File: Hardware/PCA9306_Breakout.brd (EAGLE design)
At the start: 17.8 x 10.2 mm, 15 parts

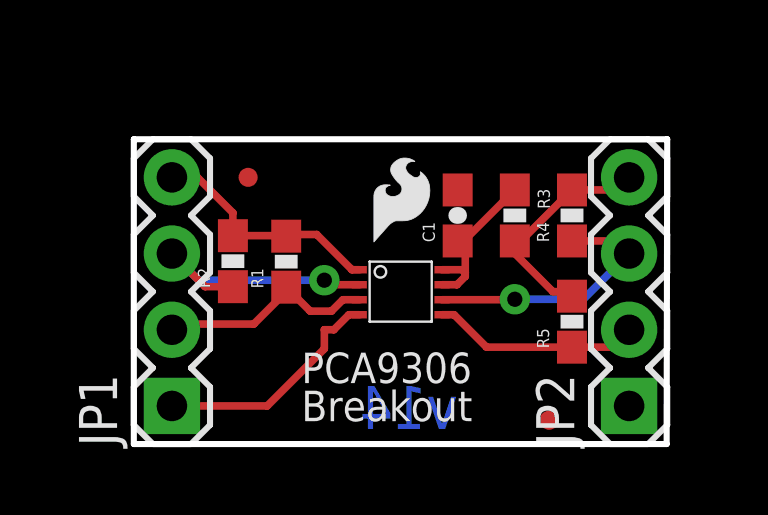
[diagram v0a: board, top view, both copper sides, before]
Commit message: Adds slik lables, adds jumper for enable pin, increases size by 10 mils in both x and y direction, updates PCA9306 to new package
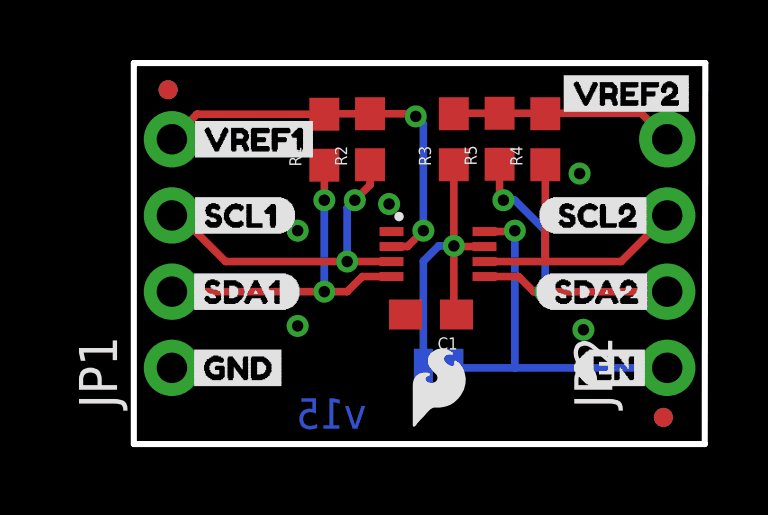
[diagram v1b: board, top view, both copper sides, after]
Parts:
- removed JP4: LOGO-SFESK, SparkFun:SFE-LOGO-FLAME
- removed JP7, JP8: FIDUCIAL1X2.5, abes:FIDUCIAL-1X2.5
- added FD1, FD2, FD3, FD4: FIDUCIALUFIDUCIAL, SparkFun-Aesthetics:FIDUCIAL-MICRO
- added LOGO2: SFE_LOGO_FLAME.1_INCH, SparkFun-Aesthetics:SFE_LOGO_FLAME_.1
- added LOGO3: SFE_LOGO_NAME.1_INCH, SparkFun-Aesthetics:SFE_LOGO_NAME_.1
- added U$10: (no value), EN:EN1
- added U$12: (no value), Product Name:LOGIC_LEVEL0
- added U$13: (no value), Product Name:TRANSLATOR1
- added U$14: (no value), Product Name:PCA93062
- added U$2: (no value), VREF1:VREF13
- added U$3: (no value), VREF1:SCL11
- added U$4: (no value), VREF1:SDA10
- added U$5: (no value), VREF1:GND2
- added U$6: (no value), VREF2:VREF20
- added U$7: (no value), VREF2:SCL22
- added U$8: (no value), VREF2:SDA21
- added U$9: (no value), EN:EN0
- C1: device SparkFun:0603-CAP -> SparkFun-Capacitors:0603
- JP1, JP2: device SparkFun:1X04 -> SparkFun-Connectors:1X04_NO_SILK
- JP3: value LOGO-SFESK -> EN; device SparkFun:SFE-LOGO-FLAME -> SparkFun-Jumpers:SMT-JUMPER_2_NC_TRACE_SILK
- R1, R2, R3, R4, R5: device SparkFun:0603-RES -> SparkFun-Resistors:0603
- U$1: value (none) -> PCA9306; device SparkFun-DigitalIC:PSOP-8 -> SparkFun-IC-Comms:VSSOP_8PIN
- moved LOGO1 6.75 mm to (15.2, 1.52)
- moved R5 6.56 mm to (12.2, 10.2)
- moved R2 6.12 mm to (7.87, 10.2)
- moved JP3 4.71 mm to (10.2, 2.54), flipped to the bottom
- moved R1 4.26 mm to (6.35, 10.1)
- moved C1 3.42 mm to (9.91, 4.32), turned to 180 degrees
- moved R3 3.25 mm to (10.7, 10.2), turned to 90 degrees
- moved R4 2.69 mm to (13.7, 10.2)
- moved JP2 1.80 mm to (17.8, 2.54)
- moved U$1 1.80 mm to (10.2, 6.35), turned to 0 degrees
- moved JP1 1.27 mm to (1.27, 2.54)
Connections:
- removed net NC: JP2.1
- removed net VREF_2: JP2.4, R3.2, R4.2, R5.2
- new net EN: JP2.1, JP3.1, U$1.P8
- new net VREF2_IN: C1.1, JP3.2, R3.1, U$1.P7
- net GND: now also U$1.P1; no longer U$1.4
- net SCL1: now also U$1.P3; no longer U$1.2
- net SCL2: now also U$1.P6; no longer U$1.6
- net SDA1: now also U$1.P4; no longer U$1.3
- net SDA2: now also U$1.P5; no longer U$1.5
- net VREF1: now also U$1.P2; no longer U$1.1
- net VREF2: now also JP2.4, R3.2, R4.2, R5.2; no longer C1.1, R3.1, U$1.7, U$1.8
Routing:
- net EN: track 0.00 -> 12.7 mm, vias 0 -> 1
- net VREF2_IN: track 0.00 -> 10.8 mm, vias 0 -> 1
- net GND: track 7.88 -> 0.00 mm, vias 0 -> 5
- net VREF_2: track 7.60 -> 0.00 mm
- net VREF1: track 8.02 -> 13.7 mm, vias 0 -> 2
- net SDA2: track 6.93 -> 11.4 mm, vias 0 -> 2
- net SDA1: track 7.41 -> 11.7 mm, vias 0 -> 2
- net SCL1: track 9.17 -> 11.5 mm, vias 1 -> 2
- net VREF2: track 5.61 -> 7.50 mm
- net SCL2: track 8.96 -> 9.95 mm, vias 1 -> 0
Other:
- board size 17.8 x 10.2 mm -> 19.1 x 12.7 mm
- board text added: "Revised by: Elias Santistevan"
- board text added: "Toni Klopfenstein"
- board text added: "Units in Inches"
- board text added: "v15"
- board text removed: "Breakout"
- board text removed: "GND"
- board text removed: "NC"
- board text removed: "PCA9306"
- board text removed: "SCL1"
- board text removed: "SCL2"
- board text removed: "SDA1"
- board text removed: "SDA2"
- board text removed: "VREF1"
- board text removed: "VREF2"
- board text removed: "v14"

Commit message: Adds an additional PTH header for GND on VREF2 side
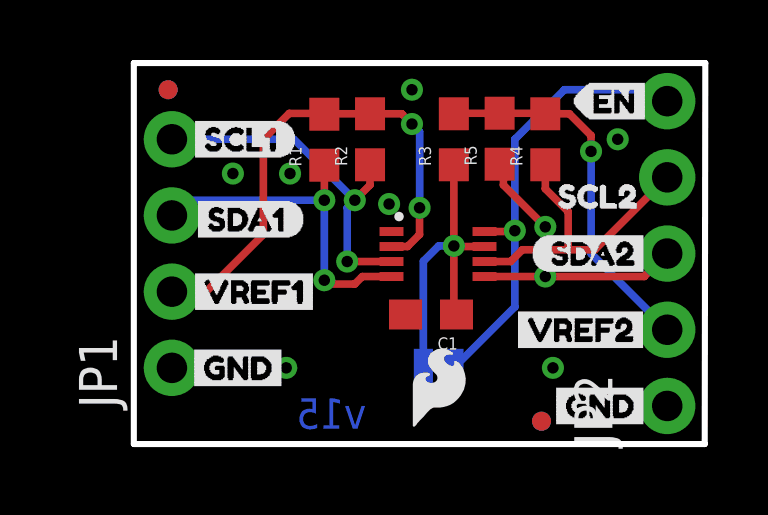
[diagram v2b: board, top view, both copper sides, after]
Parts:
- removed U$7: (no value), VREF2:SCL22
- added U$11: (no value), VREF1:GND2
- added U$15: (no value), SCL2:SCL20
- JP2: device SparkFun-Connectors:1X04_NO_SILK -> SparkFun-Connectors:1X05_NO_SILK
- moved U$9 8.89 mm to (14.6, 11.4)
- moved U$6 8.02 mm to (12.4, 3.81)
- moved U$2 5.08 mm to (1.65, 5.08)
- moved FD3 4.07 mm to (13.6, 0.76)
- moved FD4 4.07 mm to (13.6, 0.76)
- moved U$3 2.54 mm to (1.65, 10.2)
- moved U$4 2.42 mm to (1.78, 7.49)
- moved U$8 1.28 mm to (13.2, 6.35)
- moved JP2 1.27 mm to (17.8, 1.27)
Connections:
- net EN: now also JP2.5; no longer JP2.1
- net GND: now also JP2.1
- net SCL1: now also JP1.4; no longer JP1.3
- net SCL2: now also JP2.4; no longer JP2.3
- net SDA1: now also JP1.3; no longer JP1.2
- net SDA2: now also JP2.3; no longer JP2.2
- net VREF1: now also JP1.2; no longer JP1.4
- net VREF2: now also JP2.2; no longer JP2.4
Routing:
- net VREF2: track 7.50 -> 12.4 mm, vias 0 -> 1
- net VREF1: track 13.7 -> 17.4 mm
- net EN: track 12.7 -> 15.4 mm
- net SDA2: track 11.4 -> 10.8 mm

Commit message: Moves Open Hardware symbol
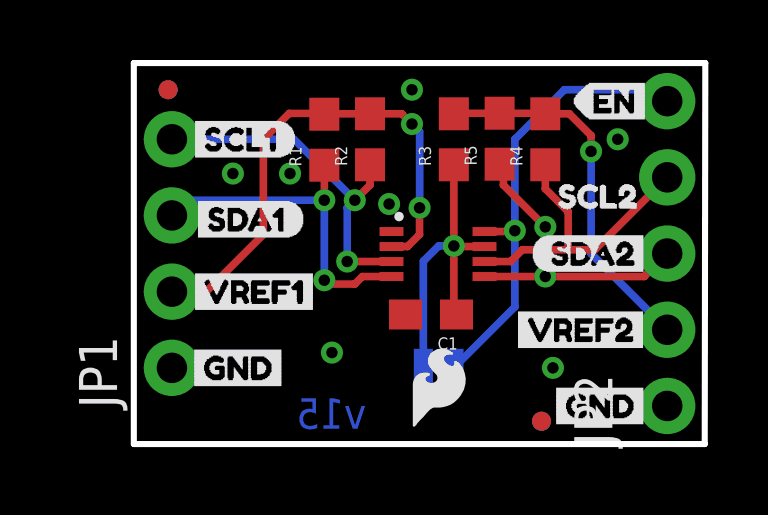
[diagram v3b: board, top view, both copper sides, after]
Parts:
- moved LOGO1 10.4 mm to (4.83, 1.52)
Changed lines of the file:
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@@
 <?xml version="1.0" encoding="utf-8"?>
 <!DOCTYPE eagle SYSTEM "eagle.dtd">
-<eagle version="9.4.2">
+<eagle version="9.4.0">
 <drawing>
 <settings>
@@
 <setting verticaltext="up"/>
 </settings>
-<grid distance="0.05" unitdist="inch" unit="inch" style="lines" multiple="1" display="yes" altdistance="0.005" altunitdist="inch" altunit="inch"/>
+<grid distance="0.01" unitdist="inch" unit="inch" style="lines" multiple="1" display="yes" altdistance="0.001" altunitdist="inch" altunit="inch"/>
 <layers>
 <layer number="1" name="Top" color="4" fill="1" visible="yes" active="yes"/>
@@
 <layer number="14" name="Route14" color="1" fill="6" visible="no" active="no"/>
 <layer number="15" name="Route15" color="4" fill="6" visible="no" active="no"/>
-<layer number="16" name="Bottom" color="1" fill="1" visible="yes" active="yes"/>
-<layer number="17" name="Pads" color="2" fill="1" visible="yes" active="yes"/>
+<layer number="16" name="Bottom" color="31" fill="1" visible="yes" active="yes"/>
+<layer number="17" name="Pads" color="30" fill="1" visible="yes" active="yes"/>
 <layer number="18" name="Vias" color="2" fill="1" visible="yes" active="yes"/>
 <layer number="19" name="Unrouted" color="6" fill="1" visible="yes" active="yes"/>
@@
 <attribute name="VALUE" x="20.955" y="0" size="1.27" layer="27" rot="R90"/>
 </element>
-<element name="LOGO1" library="SparkFun-Aesthetics" package="OSHW-LOGO-S" value="OSHW-LOGOS" x="15.24" y="1.524" smashed="yes" rot="MR0"/>
+<element name="LOGO1" library="SparkFun-Aesthetics" package="OSHW-LOGO-S" value="OSHW-LOGOS" x="4.826" y="1.524" smashed="yes" rot="MR0"/>
 <element name="FRAME1" library="SparkFun-Aesthetics" package="CREATIVE_COMMONS" value="FRAME-LETTER" x="-4.9415875" y="-10.16" smashed="yes">
 <attribute name="DESIGNER" value="" x="-4.9415875" y="-10.16" size="1.778" layer="27" display="off"/>
@@
 <contactref element="JP1" pad="1"/>
 <via x="8.509" y="8.001" extent="1-16" drill="0.381"/>
-<via x="5.08" y="2.54" extent="1-16" drill="0.381"/>
+<via x="6.604" y="3.048" extent="1-16" drill="0.381"/>
 <contactref element="JP2" pad="1"/>
 <via x="9.271" y="11.811" extent="1-16" drill="0.381"/>

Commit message: Moves passives to lower half of board, resulting in full retrace of board....
*Adds HIGH/LOW silk to board
*Adds triple jumper to correctly add enable feature
*Changes 0.1uF capacitor to 100pF capacitor
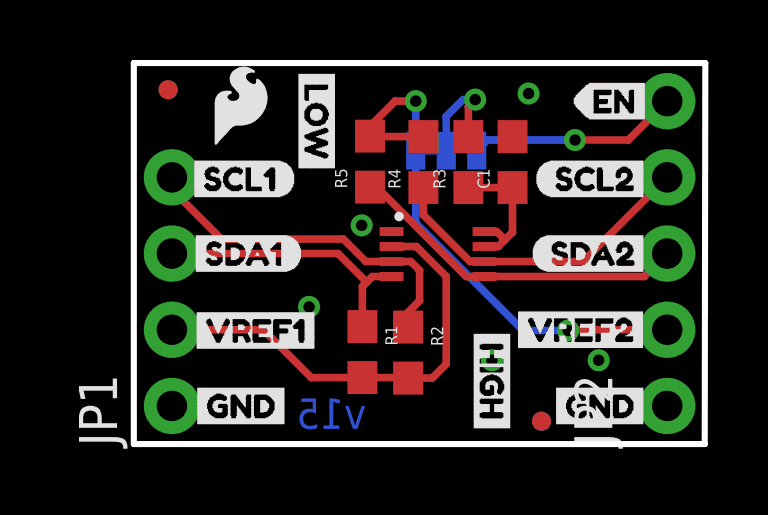
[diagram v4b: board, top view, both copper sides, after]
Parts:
- removed JP3: EN, SparkFun-Jumpers:SMT-JUMPER_2_NC_TRACE_SILK
- added JP4: EN, SparkFun-Jumpers:SMT-JUMPER_3_1-NC_TRACE_SILK
- added U$16: (no value), Jumper_Instru:CLOSE1
- added U$17, U$19: (no value), SIDE:HIGH0
- added U$18, U$20: (no value), SIDE:LOW1
- added U$7: (no value), SCL2:SCL20
- C1: value 0.1uF -> 100pF
- LOGO1: value OSHW-LOGOS -> OSHW-LOGOMINI; device SparkFun-Aesthetics:OSHW-LOGO-S -> SparkFun-Aesthetics:OSHW-LOGO-MINI
- U$15: device SCL2:SCL20 -> Jumper_Instru:CUT0
- moved LOGO2 11.5 mm to (3.56, 11.3)
- moved U$10 10.9 mm to (11.8, 11.7)
- moved LOGO1 9.33 mm to (5.64, 10.8)
- moved R2 7.22 mm to (9.14, 3.05), turned to 270 degrees
- moved R1 7.19 mm to (7.62, 3.06), turned to 270 degrees
- moved U$15 6.37 mm to (8.00, 11.5), flipped to the bottom, turned to 270 degrees
- moved C1 5.76 mm to (12.6, 9.40), turned to 90 degrees
- moved LOGO3 5.13 mm to (9.58, 5.79)
- moved U$13 5.12 mm to (13.8, 2.90)
- moved U$14 5.09 mm to (13.2, 1.52)
- moved U$12 5.08 mm to (13.9, 4.34)
- moved R5 4.38 mm to (7.87, 9.41)
- moved R4 4.13 mm to (9.65, 9.40)
- moved U$3 1.32 mm to (1.63, 8.84)
- moved U$2 1.30 mm to (1.70, 3.78)
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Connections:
- new net JUMPER_IN: JP4.2, R3.2
- net EN: now also JP4.1; no longer JP3.1, U$1.P8
- net VREF2: now also JP4.3; no longer R3.2
- net VREF2_IN: now also U$1.P8; no longer JP3.2
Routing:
- net EN: track 15.4 -> 7.03 mm
- net VREF2_IN: track 10.8 -> 4.89 mm, vias 1 -> 0
- net VREF2: track 12.4 -> 17.9 mm, vias 1 -> 2
- net JUMPER_IN: track 0.00 -> 3.67 mm, vias 0 -> 1
- net VREF1: track 17.4 -> 15.2 mm, vias 2 -> 0
- net SDA1: track 11.5 -> 9.33 mm, vias 2 -> 0
- net SDA2: track 10.8 -> 11.5 mm, vias 2 -> 0
- net SCL1: track 12.0 -> 11.8 mm, vias 2 -> 0

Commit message: Updates silk on jumper and "HIGH" and "LOW" voltages on bottom, renumbers parts in schematic
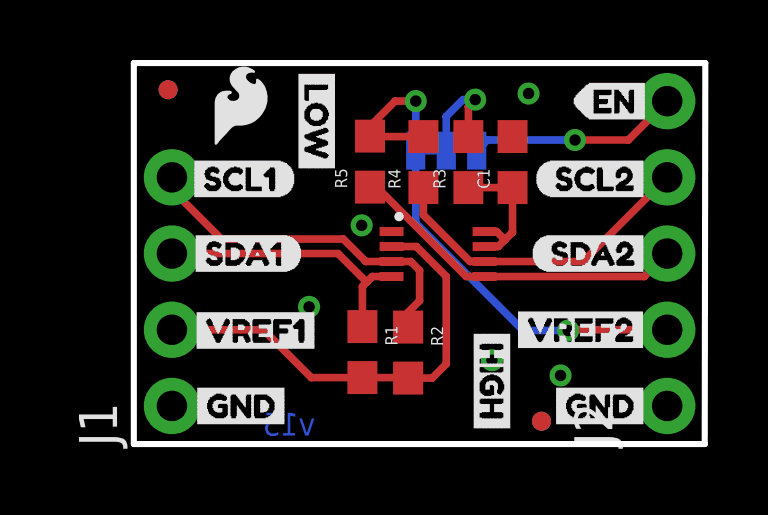
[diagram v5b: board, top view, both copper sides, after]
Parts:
- removed JP4: EN, SparkFun-Jumpers:SMT-JUMPER_3_1-NC_TRACE_SILK
- added J1: (no value), SparkFun-Connectors:1X04_NO_SILK
- added U$21: (no value), Voltages:1#2V#3#3V0
- added U$22: (no value), Voltages:1#8V#5V1
- JP1: value (none) -> EN; device SparkFun-Connectors:1X04_NO_SILK -> SparkFun-Jumpers:SMT-JUMPER_3_1-NC_TRACE_SILK
- LOGO2: value SFE_LOGO_FLAME.1_INCH -> SFE_LOGO_NAME.1_INCH; device SparkFun-Aesthetics:SFE_LOGO_FLAME_.1 -> SparkFun-Aesthetics:SFE_LOGO_NAME_.1
- LOGO3: value SFE_LOGO_NAME.1_INCH -> SFE_LOGO_FLAME.1_INCH; device SparkFun-Aesthetics:SFE_LOGO_NAME_.1 -> SparkFun-Aesthetics:SFE_LOGO_FLAME_.1
- R1, R2, R4, R5: value 1k -> 2.2k
- U$15: device Jumper_Instru:CUT0 -> Jumper_Options:ON2
- U$16: device Jumper_Instru:CLOSE1 -> Jumper_Options:SWCH0
- moved FD2 16.6 mm to (13.6, 0.76), flipped to the top
- moved FD3 16.6 mm to (1.14, 11.8)
- moved JP1 12.5 mm to (10.4, 9.78), flipped to the bottom, turned to 0 degrees
- moved LOGO2 8.16 mm to (9.58, 5.79), flipped to the bottom
- moved LOGO3 8.16 mm to (3.56, 11.3), flipped to the top
- moved U$16 4.70 mm to (12.9, 7.47), turned to 90 degrees
- moved U$15 3.35 mm to (7.90, 8.18), turned to 90 degrees
- flipped FD1 to the bottom
- renumbered JP2 to J2, U$1 to U1
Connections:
- net EN: now also JP1.1; no longer JP4.1
- net GND: now also J1.1; no longer JP1.1
- net JUMPER_IN: now also JP1.2; no longer JP4.2
- net SCL1: now also J1.4; no longer JP1.4
- net SDA1: now also J1.3; no longer JP1.3
- net VREF1: now also J1.2; no longer JP1.2
- net VREF2: now also JP1.3; no longer JP4.3

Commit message: Fixes traces for both data lines, corrects punctuation of schematic note.
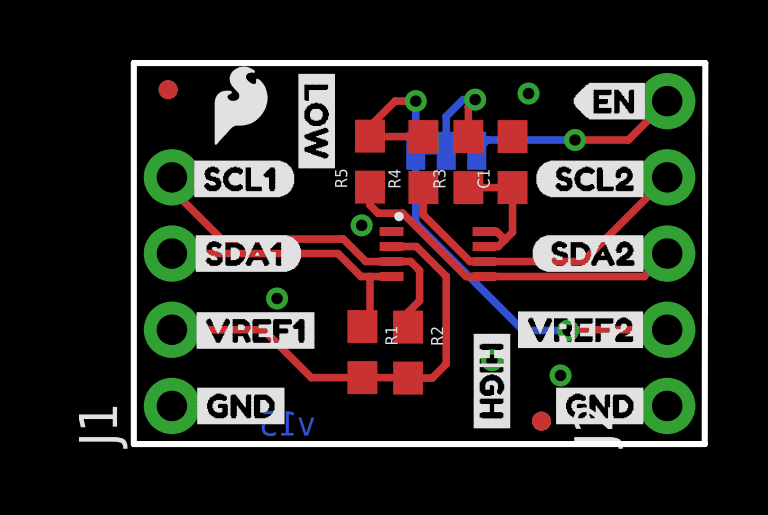
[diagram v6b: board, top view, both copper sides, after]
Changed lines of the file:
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@@
 <layer number="115" name="ReferenceISLANDS" color="7" fill="1" visible="no" active="no"/>
 <layer number="116" name="Patch_BOT" color="9" fill="4" visible="no" active="yes"/>
-<layer number="117" name="PM_Ref" color="26" fill="1" visible="yes" active="yes"/>
+<layer number="117" name="PM_Ref" color="26" fill="1" visible="no" active="yes"/>
 <layer number="118" name="Rect_Pads" color="7" fill="1" visible="no" active="no"/>
-<layer number="119" name="PF_Ref" color="31" fill="1" visible="yes" active="yes"/>
-<layer number="120" name="WFL_Ref" color="25" fill="1" visible="yes" active="yes"/>
+<layer number="119" name="PF_Ref" color="31" fill="1" visible="no" active="yes"/>
+<layer number="120" name="WFL_Ref" color="25" fill="1" visible="no" active="yes"/>
 <layer number="121" name="_tsilk" color="7" fill="1" visible="no" active="yes"/>
 <layer number="122" name="_bsilk" color="7" fill="1" visible="no" active="yes"/>
@@
 <wire x1="19.05" y1="12.7" x2="0" y2="12.7" width="0.2032" layer="20"/>
 <wire x1="0" y1="12.7" x2="0" y2="0" width="0.2032" layer="20"/>
-<text x="6.0452" y="0.2794" size="0.762" layer="16" font="vector" ratio="12" rot="MR0">v15</text>
+<text x="6.0452" y="0.2794" size="0.8128" layer="16" font="vector" ratio="12" rot="MR0">v15</text>
 <text x="25.4" y="-10.16" size="1.778" layer="27" font="vector" ratio="15">T. Klopfenstein</text>
 <dimension x1="0" y1="12.7" x2="19.05" y2="12.7" x3="9.525" y3="13.97" textsize="1.778" layer="47" unit="inch"/>
@@
 <contactref element="R1" pad="1"/>
 <contactref element="J1" pad="3"/>
-<wire x1="8.59" y1="5.584" x2="7.9502" y2="5.584" width="0.254" layer="1"/>
-<wire x1="7.9502" y1="5.584" x2="7.7617" y2="5.3955" width="0.254" layer="1"/>
-<wire x1="7.7617" y1="5.3955" x2="7.62" y2="5.2538" width="0.254" layer="1"/>
-<wire x1="7.62" y1="5.2538" x2="7.62" y2="3.914" width="0.254" layer="1"/>
 <wire x1="1.27" y1="6.35" x2="6.8072" y2="6.35" width="0.254" layer="1"/>
-<wire x1="6.8072" y1="6.35" x2="7.7617" y2="5.3955" width="0.254" layer="1"/>
+<wire x1="6.8072" y1="6.35" x2="7.5732" y2="5.584" width="0.254" layer="1"/>
+<wire x1="7.5732" y1="5.584" x2="7.874" y2="5.584" width="0.254" layer="1"/>
+<wire x1="7.874" y1="5.584" x2="8.59" y2="5.584" width="0.254" layer="1"/>
+<wire x1="7.874" y1="5.584" x2="7.874" y2="4.168" width="0.254" layer="1"/>
+<wire x1="7.874" y1="4.168" x2="7.62" y2="3.914" width="0.254" layer="1"/>
 </signal>
 <signal name="GND">
@@
 <contactref element="J2" pad="1"/>
 <via x="7.5946" y="7.2898" extent="1-16" drill="0.381"/>
-<via x="5.842" y="4.572" extent="1-16" drill="0.381"/>
+<via x="4.7752" y="4.8514" extent="1-16" drill="0.381"/>
 <via x="11.938" y="2.794" extent="1-16" drill="0.381"/>
 <via x="13.1572" y="11.684" extent="1-16" drill="0.381"/>
@@
 <contactref element="R5" pad="1"/>
 <contactref element="J2" pad="3"/>
-<wire x1="11.69" y1="5.584" x2="11.0784" y2="5.584" width="0.254" layer="1"/>
-<wire x1="8.0984" y1="8.564" x2="7.874" y2="8.564" width="0.254" layer="1"/>
-<wire x1="11.0784" y1="5.584" x2="8.0984" y2="8.564" width="0.254" layer="1"/>
 <wire x1="11.69" y1="5.584" x2="17.014" y2="5.584" width="0.254" layer="1"/>
 <wire x1="17.014" y1="5.584" x2="17.78" y2="6.35" width="0.254" layer="1"/>
+<wire x1="7.874" y1="8.564" x2="7.874" y2="7.9623125" width="0.254" layer="1"/>
+<wire x1="8.1431125" y1="7.6932" x2="8.9662" y2="7.6932" width="0.254" layer="1"/>
+<wire x1="11.69" y1="5.584" x2="11.0754" y2="5.584" width="0.254" layer="1"/>
+<wire x1="11.0754" y1="5.584" x2="8.9662" y2="7.6932" width="0.254" layer="1"/>
+<wire x1="7.874" y1="7.9623125" x2="8.1431125" y2="7.6932" width="0.254" layer="1"/>
 </signal>
 <signal name="VREF1">
